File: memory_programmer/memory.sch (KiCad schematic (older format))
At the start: 2 parts, among them U1 AT28C256-15PU, U2 AT28C256-15PU

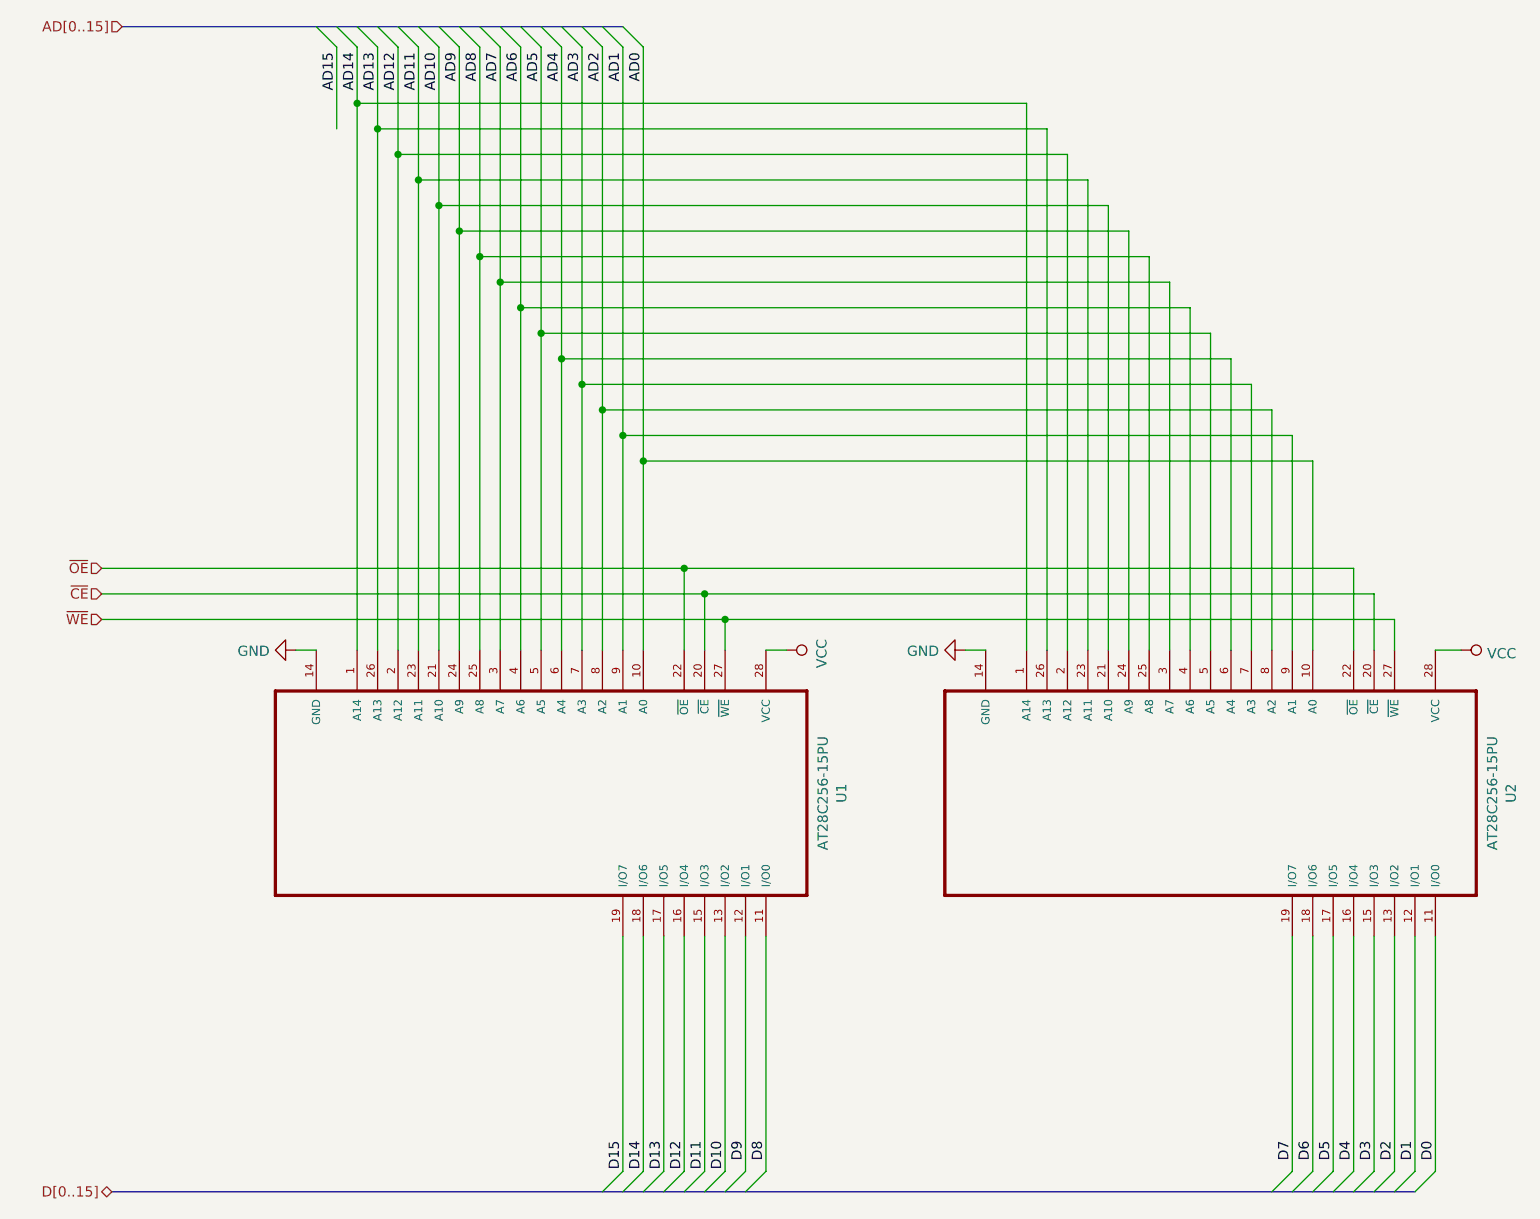
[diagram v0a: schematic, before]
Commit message: memory programmer and cu
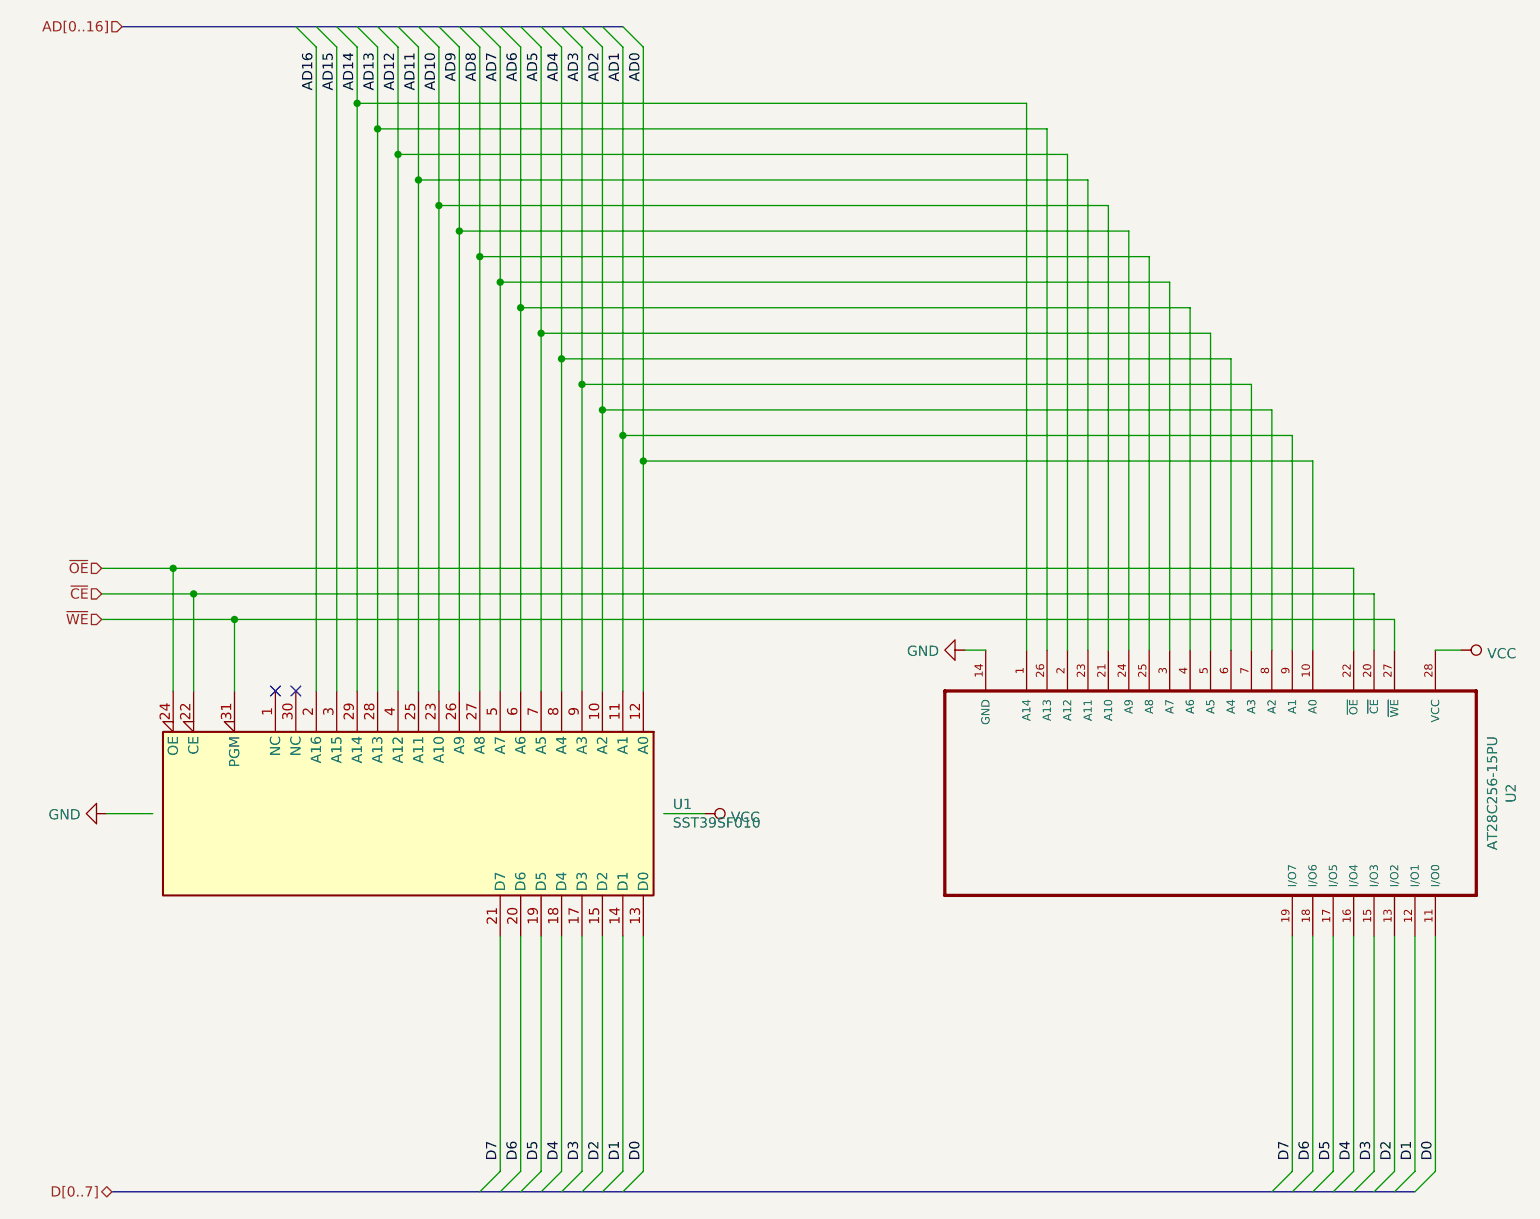
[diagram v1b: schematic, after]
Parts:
- removed U1: AT28C256-15PU, Package_DIP:DIP-28_W7.62mm_Socket_LongPads, symbol AT28C256-15PU:AT28C256-15PU
- added U1: SST39SF010, Package_DIP:DIP-32_W15.24mm_Socket_LongPads, symbol Memory_Flash:SST39SF010
- U2: footprint Package_DIP:DIP-28_W7.62mm_Socket_LongPads -> Package_DIP:DIP-28_W15.24mm_Socket_LongPads
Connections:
- net AD0: now also U1.12 (A0)
- net AD1: now also U1.11 (A1)
- net AD10: now also U1.23 (A10)
- net AD11: now also U1.25 (A11)
- net AD12: now also U1.4 (A12)
- net AD13: now also U1.28 (A13)
- net AD14: now also U1.29 (A14)
- net AD15: now also U1.3 (A15)
- net AD2: now also U1.10 (A2)
- net AD3: now also U1.9 (A3)
- net AD4: now also U1.8 (A4)
- net AD5: now also U1.7 (A5)
- net AD6: now also U1.6 (A6)
- net AD7: now also U1.5 (A7)
- net AD8: now also U1.27 (A8)
- net AD9: now also U1.26 (A9)
- net D0: now also U1.13 (D0)
- net D1: now also U1.14 (D1)
- net D2: now also U1.15 (D2)
- net D3: now also U1.17 (D3)
- net D4: now also U1.18 (D4)
- net D5: now also U1.19 (D5)
- net D6: now also U1.20 (D6)
- net D7: now also U1.21 (D7)
- net GND: now also U1.16 (GND)
- net VCC: now also U1.32 (VCC)
- net ~CE~: now also U1.22 (CE)
- net ~OE~: now also U1.24 (OE)
- net ~WE~: now also U1.31 (PGM)
- new net AD16: U1.2 (A16)
- no-connect marks 0 -> 2
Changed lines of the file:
@@
 $Descr A4 11693 8268
 encoding utf-8
-Sheet 4 5
+Sheet 2 3
 Title ""
 Date ""
@@
 F 0 "U2" H 6600 5770 50  0000 C CNN
 F 1 "AT28C256-15PU" H 6600 5679 50  0000 C CNN
-F 2 "Package_DIP:DIP-28_W7.62mm_Socket_LongPads" H 6600 4400 50  0001 L BNN
+F 2 "Package_DIP:DIP-28_W15.24mm_Socket_LongPads" H 6600 4400 50  0001 L BNN
 F 3 "" H 6600 4400 50  0001 L BNN
 F 4 "AT28C256-15PU" H 6600 4400 50  0001 L BNN "Field4"
@@
 	0    1    1    0
 $EndComp
-$Comp
-L AT28C256-15PU:AT28C256-15PU U?
-U 1 1 5D37830F
-P 3325 4400
-AR Path="/5D35D52D/5D37830F" Ref="U?"  Part="1"
-AR Path="/5D35D52D/5D367E7A/5D37830F" Ref="U?"  Part="1"
-AR Path="/5EE1C593/5D37830F" Ref="U1"  Part="1"
-F 0 "U1" H 3325 5770 50  0000 C CNN
-F 1 "AT28C256-15PU" H 3325 5679 50  0000 C CNN
-F 2 "Package_DIP:DIP-28_W7.62mm_Socket_LongPads" H 3325 4400 50  0001 L BNN
-F 3 "" H 3325 4400 50  0001 L BNN
-F 4 "AT28C256-15PU" H 3325 4400 50  0001 L BNN "Field4"
-F 5 "AT28C256 Series 256 Kb _32 K x 8_ 5.5 V Paged Parallel EEPROM - DIP-28" H 3325 4400 50  0001 L BNN "Field5"
-F 6 "Unavailable" H 3325 4400 50  0001 L BNN "Field6"
-F 7 "DIP-28 Microchip" H 3325 4400 50  0001 L BNN "Field7"
-F 8 "Microchip" H 3325 4400 50  0001 L BNN "Field8"
-	1    3325 4400
-	0    1    1    0
-$EndComp
 Text HLabel 1175 650  0    50   Input ~ 0
-AD[0..15]
-$Comp
-L power:VCC #PWR?
-U 1 1 5D378316
-P 4425 3700
-AR Path="/5D35D52D/5D378316" Ref="#PWR?"  Part="1"
-AR Path="/5D35D52D/5D367E7A/5D378316" Ref="#PWR?"  Part="1"
-AR Path="/5EE1C593/5D378316" Ref="#PWR08"  Part="1"
-F 0 "#PWR08" H 4425 3550 50  0001 C CNN
-F 1 "VCC" H 4442 3873 50  0000 C CNN
-F 2 "" H 4425 3700 50  0001 C CNN
-F 3 "" H 4425 3700 50  0001 C CNN
-	1    4425 3700
-	0    1    1    0
-$EndComp
-Wire Wire Line
-	4425 3700 4325 3700
+AD[0..16]
 $Comp
 L power:VCC #PWR?
@@
 Wire Wire Line
 	5300 3700 5400 3700
-Wire Wire Line
-	2025 3700 2125 3700
 $Comp
 L power:GND #PWR?
 U 1 1 5D37832C
-P 2025 3700
+P 1100 4500
 AR Path="/5D35D52D/5D37832C" Ref="#PWR?"  Part="1"
 AR Path="/5D35D52D/5D367E7A/5D37832C" Ref="#PWR?"  Part="1"
 AR Path="/5EE1C593/5D37832C" Ref="#PWR07"  Part="1"
-F 0 "#PWR07" H 2025 3450 50  0001 C CNN
-F 1 "GND" V 2030 3572 50  0000 R CNN
-F 2 "" H 2025 3700 50  0001 C CNN
-F 3 "" H 2025 3700 50  0001 C CNN
-	1    2025 3700
+F 0 "#PWR07" H 1100 4250 50  0001 C CNN
+F 1 "GND" V 1105 4372 50  0000 R CNN
+F 2 "" H 1100 4500 50  0001 C CNN
+F 3 "" H 1100 4500 50  0001 C CNN
+	1    1100 4500
 	0    1    1    0
 $EndComp
@@
 	7000 2775 7000 3700
 Wire Wire Line
-	2325 3700 2325 1025
-Wire Wire Line
-	2425 1150 2425 3700
-Wire Wire Line
-	2525 3700 2525 1275
-Wire Wire Line
-	2625 3700 2625 1400
-Wire Wire Line
-	2725 1525 2725 3700
-Wire Wire Line
-	2825 3700 2825 1650
-Wire Wire Line
-	2925 1775 2925 3700
-Wire Wire Line
-	3025 3700 3025 1900
-Wire Wire Line
-	3125 2025 3125 3700
-Wire Wire Line
-	3325 2275 3325 3700
+	2325 3900 2325 1025
+Wire Wire Line
+	2425 1150 2425 3900
+Wire Wire Line
+	2525 3900 2525 1275
+Wire Wire Line
+	2625 3900 2625 1400
+Wire Wire Line
+	2725 1525 2725 3900
+Wire Wire Line
+	2825 3900 2825 1650
+Wire Wire Line
+	2925 1775 2925 3900
+Wire Wire Line
+	3025 3900 3025 1900
+Wire Wire Line
+	3125 2025 3125 3900
+Wire Wire Line
+	3325 2275 3325 3900
 Connection ~ 3325 2275
 Connection ~ 3125 2025
@@
 Connection ~ 2425 1150
 Connection ~ 2325 1025
-Entry Wire Line
-	2125 650  2225 750
-Wire Wire Line
-	2225 750  2225 1150
 Text Label 2225 775  3    50   ~ 0
 AD15
@@
 Text Label 6900 6100 3    50   ~ 0
 D7
-Entry Wire Line
-	4325 6250 4225 6350
-Text Label 4325 6100 3    50   ~ 0
-D8
-Entry Wire Line
-	4225 6250 4125 6350
-Text Label 4225 6100 3    50   ~ 0
-D9
-Entry Wire Line
-	4125 6250 4025 6350
-Text Label 4125 6100 3    50   ~ 0
-D10
-Entry Wire Line
-	4025 6250 3925 6350
-Text Label 4025 6100 3    50   ~ 0
-D11
-Entry Wire Line
-	3925 6250 3825 6350
-Text Label 3925 6100 3    50   ~ 0
-D12
-Entry Wire Line
-	3825 6250 3725 6350
-Text Label 3825 6100 3    50   ~ 0
-D13
-Entry Wire Line
-	3725 6250 3625 6350
-Text Label 3725 6100 3    50   ~ 0
-D14
-Entry Wire Line
-	3625 6250 3525 6350
-Text Label 3625 6100 3    50   ~ 0
-D15
 Text HLabel 1125 6350 0    50   BiDi ~ 0
-D[0..15]
+D[0..7]
 Connection ~ 3225 2150
 Wire Wire Line
-	3225 2150 3225 3700
+	3225 2150 3225 3900
 Connection ~ 3425 2400
 Connection ~ 3525 2525
@@
 	3725 750  3725 2775
 Wire Wire Line
-	3725 2775 3725 3700
+	3725 2775 3725 3900
 Wire Wire Line
 	3625 750  3625 2650
 Wire Wire Line
-	3625 2650 3625 3700
+	3625 2650 3625 3900
 Wire Wire Line
 	3525 750  3525 2525
 Wire Wire Line
-	3525 2525 3525 3700
+	3525 2525 3525 3900
 Wire Wire Line
 	3425 750  3425 2400
 Wire Wire Line
-	3425 2400 3425 3700
+	3425 2400 3425 3900
 Wire Wire Line
 	3725 2775 7000 2775
@@
 	6800 2525 3525 2525
 Wire Wire Line
-	4125 3700 4125 3550
-Wire Wire Line
 	7400 3700 7400 3550
 Wire Wire Line
 	7300 3700 7300 3425
-Wire Wire Line
-	4025 3700 4025 3425
-Wire Wire Line
-	3925 3300 3925 3700
-Wire Wire Line
-	3925 3300 7200 3300
 Wire Wire Line
 	7200 3300 7200 3700
@@
 ~WE~
 Wire Wire Line
-	1075 3550 4125 3550
-Connection ~ 4125 3550
-Wire Wire Line
-	4125 3550 7400 3550
-Wire Wire Line
-	1075 3425 4025 3425
-Connection ~ 4025 3425
-Wire Wire Line
-	4025 3425 7300 3425
+	1075 3425 1525 3425
 Text HLabel 1075 3425 0    50   Input ~ 0
 ~CE~
-Wire Wire Line
-	3925 3300 1075 3300
-Connection ~ 3925 3300
 Text HLabel 1075 3300 0    50   Input ~ 0
 ~OE~
@@
 	7000 5100 7000 6250
 Wire Wire Line
+	6900 5100 6900 6250
+Entry Wire Line
+	3725 6250 3625 6350
+Text Label 3725 6100 3    50   ~ 0
+D0
+Entry Wire Line
+	3625 6250 3525 6350
+Text Label 3625 6100 3    50   ~ 0
+D1
+Entry Wire Line
+	3525 6250 3425 6350
+Text Label 3525 6100 3    50   ~ 0
+D2
+Entry Wire Line
+	3425 6250 3325 6350
+Text Label 3425 6100 3    50   ~ 0
+D3
+Entry Wire Line
+	3325 6250 3225 6350
+Text Label 3325 6100 3    50   ~ 0
+D4
+Entry Wire Line
+	3225 6250 3125 6350
+Text Label 3225 6100 3    50   ~ 0
+D5
+Entry Wire Line
+	3125 6250 3025 6350
+Text Label 3125 6100 3    50   ~ 0
+D6
+Entry Wire Line
+	3025 6250 2925 6350
+Text Label 3025 6100 3    50   ~ 0
+D7
+Wire Wire Line
+	3725 5100 3725 6250
+Wire Wire Line
 	3625 5100 3625 6250
 Wire Wire Line
-	3825 5100 3825 6250
-Wire Wire Line
-	3925 5100 3925 6250
-Wire Wire Line
-	4025 5100 4025 6250
-Wire Wire Line
-	4125 5100 4125 6250
-Wire Wire Line
-	4225 5100 4225 6250
-Wire Wire Line
-	4325 5100 4325 6250
-Wire Wire Line
-	3725 5100 3725 6250
-Wire Wire Line
-	6900 5100 6900 6250
+	3525 5100 3525 6250
+Wire Wire Line
+	3425 5100 3425 6250
+Wire Wire Line
+	3325 5100 3325 6250
+Wire Wire Line
+	3225 5100 3225 6250
+Wire Wire Line
+	3125 5100 3125 6250
+Wire Wire Line
+	3025 5100 3025 6250
+Wire Wire Line
+	1100 4500 1325 4500
+$Comp
+L power:VCC #PWR0101
+U 1 1 5F47D569
+P 4025 4500
+F 0 "#PWR0101" H 4025 4350 50  0001 C CNN
+F 1 "VCC" V 4042 4628 50  0000 L CNN
+F 2 "" H 4025 4500 50  0001 C CNN
+F 3 "" H 4025 4500 50  0001 C CNN
+	1    4025 4500
+	0    1    1    0
+$EndComp
+Wire Wire Line
+	4025 4500 3825 4500
+Wire Wire Line
+	2225 750  2225 3900
+Entry Wire Line
+	2025 650  2125 750
+Text Label 2125 775  3    50   ~ 0
+AD16
+Entry Wire Line
+	2125 650  2225 750
+Wire Wire Line
+	1525 3900 1525 3425
+Connection ~ 1525 3425
+Wire Wire Line
+	1425 3900 1425 3300
+Connection ~ 1425 3300
+Wire Wire Line
+	1425 3300 1075 3300
+Wire Wire Line
+	1725 3900 1725 3550
+Wire Wire Line
+	1075 3550 1725 3550
+Connection ~ 1725 3550
+$Comp
+L Memory_Flash:SST39SF010 U1
+U 1 1 5F45B906
+P 2525 4500
+F 0 "U1" V 2479 5844 50  0000 L CNN
+F 1 "SST39SF010" V 2570 5844 50  0000 L CNN
+F 2 "Package_DIP:DIP-32_W15.24mm_Socket_LongPads" H 2525 4800 50  0001 C CNN
+F 3 "http://ww1.microchip.com/downloads/en/DeviceDoc/25022B.pdf" H 2525 4800 50  0001 C CNN
+	1    2525 4500
+	0    1    1    0
+$EndComp
+NoConn ~ 1925 3900
+NoConn ~ 2025 3900
+Wire Wire Line
+	1725 3550 7400 3550
+Wire Wire Line
+	1525 3425 7300 3425
+Wire Wire Line
+	1425 3300 7200 3300
+Wire Wire Line
+	2125 3900 2125 750
+Wire Bus Line
+	1175 650  3625 650
 Wire Bus Line
 	1125 6350 7500 6350
-Wire Bus Line
-	1175 650  3625 650
 $EndSCHEMATC
